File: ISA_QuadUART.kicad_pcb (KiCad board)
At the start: 2 copper layers, 104.1 x 102.9 mm, 41 parts, among them J1 ISA BUS, J11 Serial 4 IDC, J12 Serial 3 IDC, J13 UART4_SEL, J2 ADDR_IRQ, J3 UART1_SEL, J4 UART2_SEL, J5 ADDR, J7 Serial 1 DB9, J8 UART3_SEL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

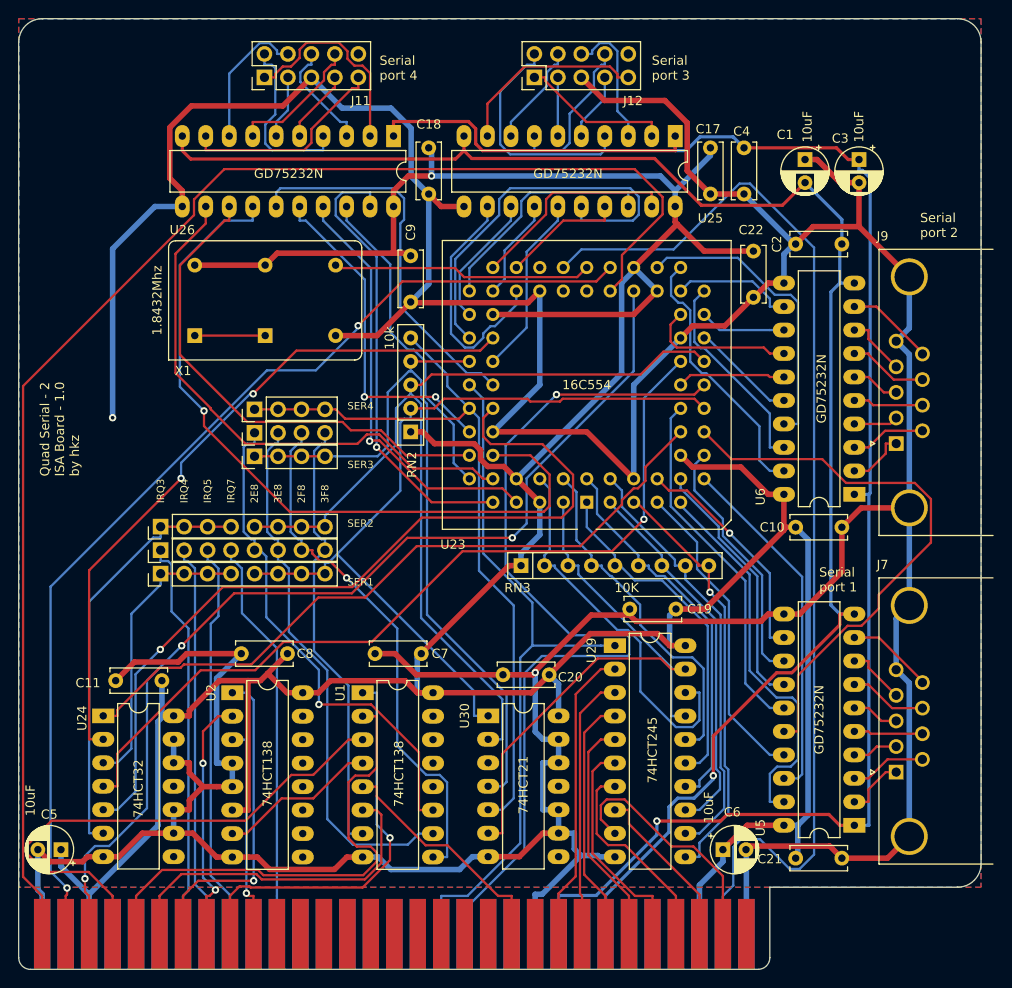
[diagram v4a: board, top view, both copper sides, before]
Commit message: Change ground plane on board
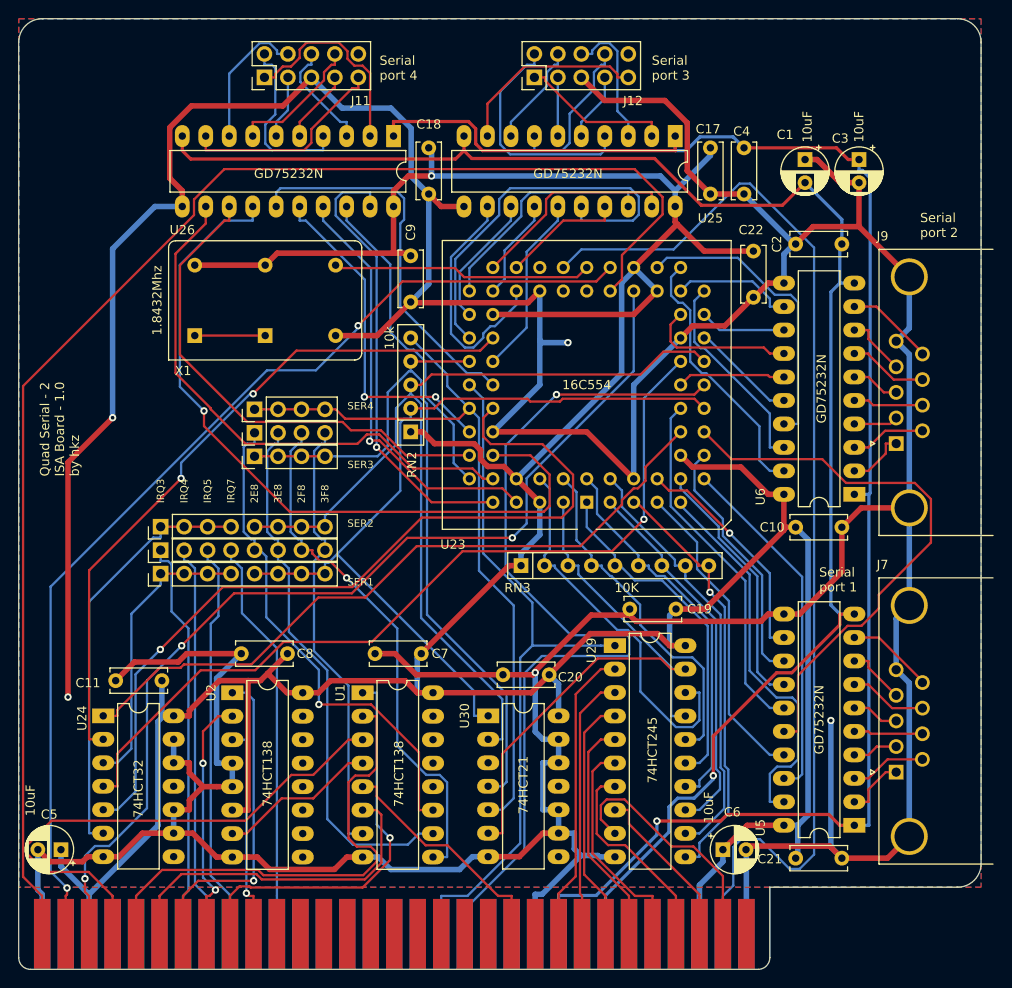
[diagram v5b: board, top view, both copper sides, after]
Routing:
- net GND: track 573.0 -> 623.8 mm, vias 2 -> 5

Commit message: Slight fixes to silkscreen
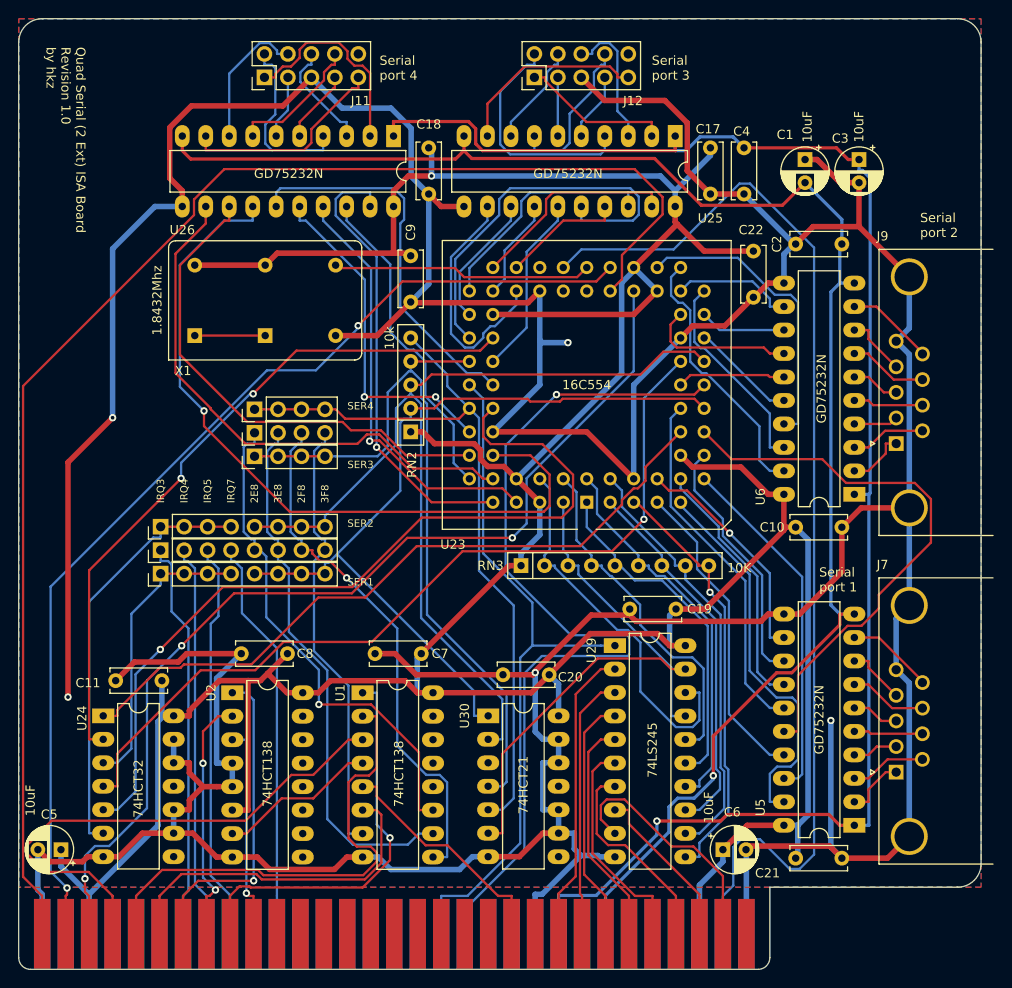
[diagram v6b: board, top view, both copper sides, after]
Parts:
- U29: value 74HCT245 -> 74LS245
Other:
- board text added: "Quad Serial (2 Ext) ISA Board Revision 1.0 by hkz"
- board text removed: "Quad Serial - 2 ISA Board - 1.0 by hkz"

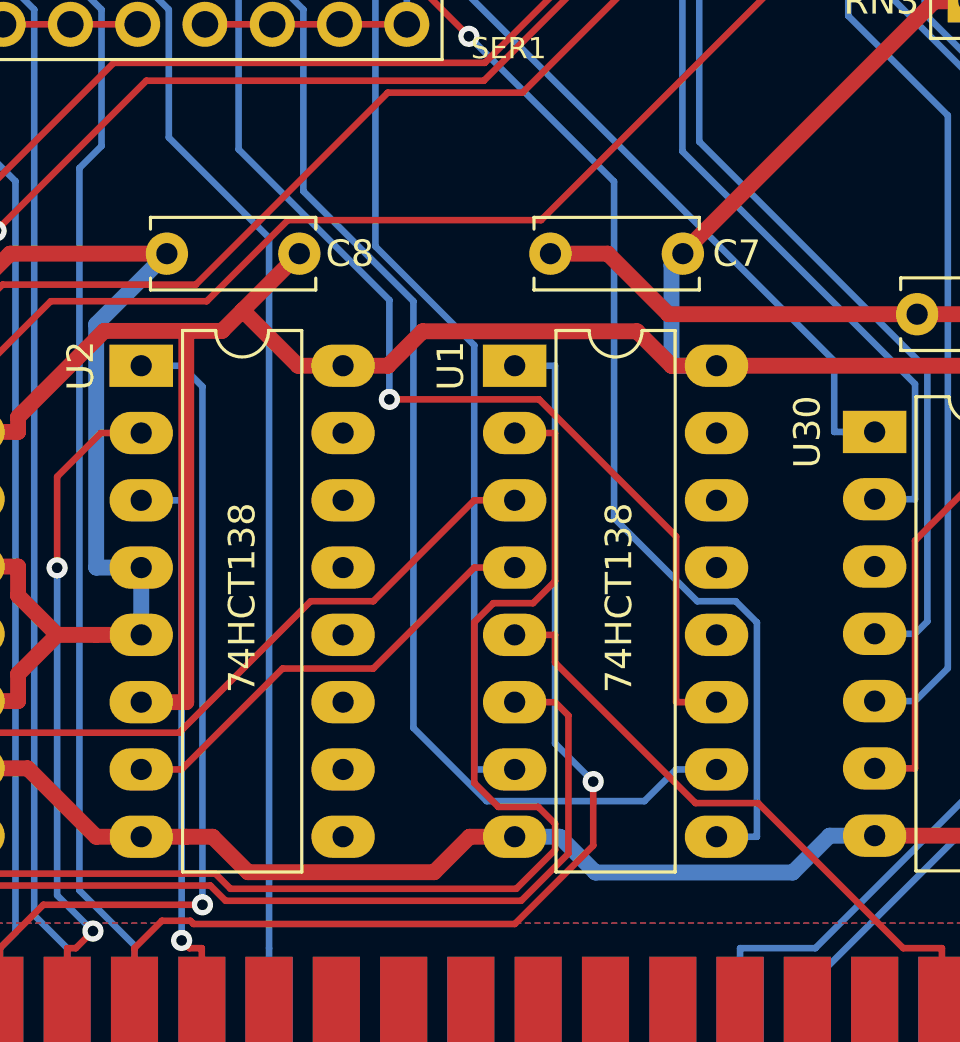
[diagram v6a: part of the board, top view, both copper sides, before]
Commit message: Slightly better filling for ground plane
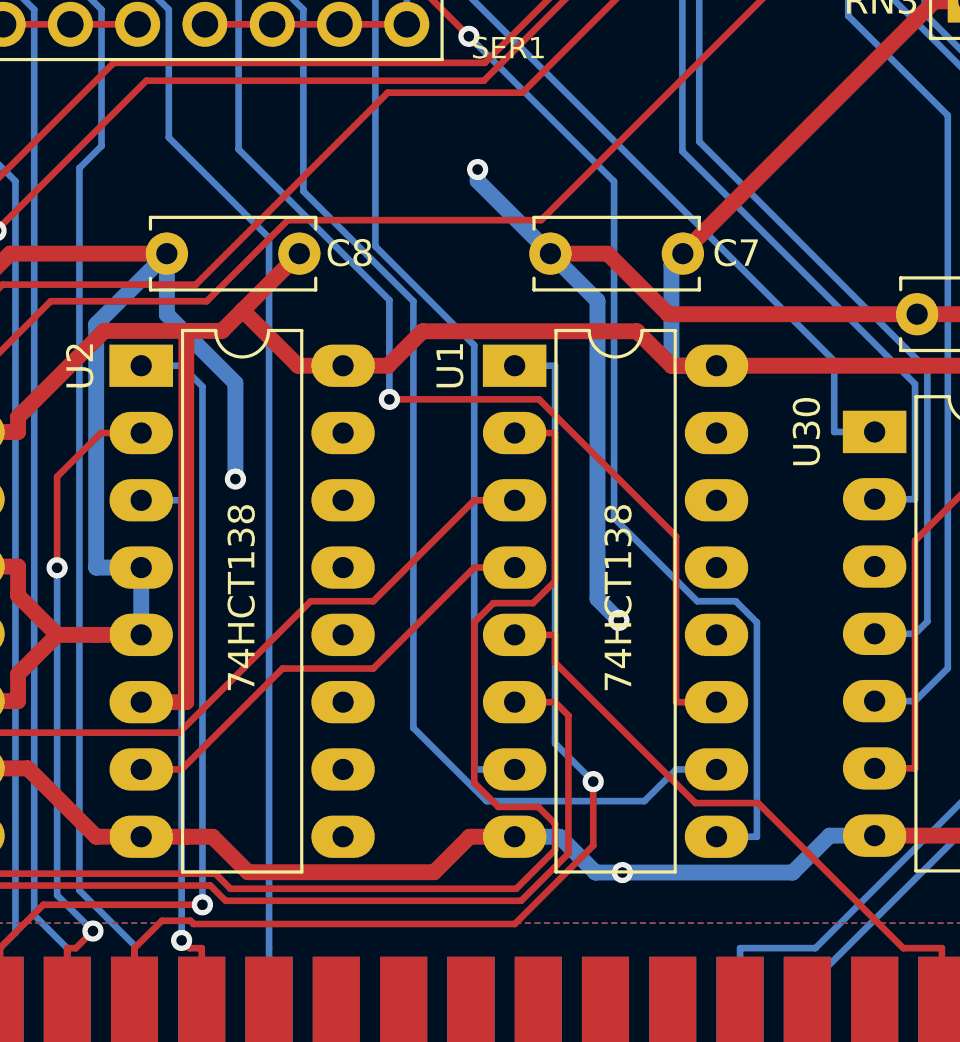
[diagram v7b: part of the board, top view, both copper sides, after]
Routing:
- net GND: track 623.8 -> 652.6 mm, vias 5 -> 9
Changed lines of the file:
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@@
     (thickness 1.6)
     (drawings 30)
-    (tracks 1300)
+    (tracks 1313)
     (zones 0)
     (modules 41)
@@
   (page A3)
   (layers
-    (0 F.Cu signal hide)
-    (31 B.Cu signal hide)
+    (0 F.Cu signal)
+    (31 B.Cu signal)
     (32 B.Adhes user)
     (33 F.Adhes user)
@@
   (segment (start 261.62 191.008) (end 259.9197 191.008) (width 0.6) (layer B.Cu) (net 2))
   (segment (start 259.9197 191.008) (end 258.5285 192.3992) (width 0.6) (layer B.Cu) (net 2))
-  (segment (start 258.5285 192.3992) (end 251.0825 192.3992) (width 0.6) (layer B.Cu) (net 2))
+  (segment (start 258.5285 192.3992) (end 252.1008 192.3992) (width 0.6) (layer B.Cu) (net 2))
   (segment (start 251.0825 192.3992) (end 249.7313 191.048) (width 0.6) (layer B.Cu) (net 2))
   (segment (start 246.3307 191.048) (end 244.9913 192.3874) (width 0.6) (layer F.Cu) (net 2))
@@
   (segment (start 216.154 148.336) (end 220.98 143.51) (width 0.6) (layer F.Cu) (net 2))
   (segment (start 216.154 173.736) (end 216.154 148.336) (width 0.6) (layer F.Cu) (net 2))
+  (via (at 246.634 165.862) (size 0.8) (drill 0.4) (layers F.Cu B.Cu) (net 2))
+  (segment (start 246.634 166.29) (end 249.381 169.037) (width 0.6) (layer B.Cu) (net 2))
+  (segment (start 246.634 165.862) (end 246.634 166.29) (width 0.6) (layer B.Cu) (net 2))
+  (via (at 251.968 182.88) (size 0.8) (drill 0.4) (layers F.Cu B.Cu) (net 2))
+  (segment (start 251.15819 170.81419) (end 249.381 169.037) (width 0.6) (layer B.Cu) (net 2))
+  (segment (start 251.15819 182.07019) (end 251.15819 170.81419) (width 0.6) (layer B.Cu) (net 2))
+  (segment (start 251.968 182.88) (end 251.15819 182.07019) (width 0.6) (layer B.Cu) (net 2))
+  (via (at 237.49 177.546) (size 0.8) (drill 0.4) (layers F.Cu B.Cu) (net 2))
+  (segment (start 234.903 171.336998) (end 234.903 169.037) (width 0.6) (layer B.Cu) (net 2))
+  (segment (start 237.49 173.923998) (end 234.903 171.336998) (width 0.6) (layer B.Cu) (net 2))
+  (segment (start 237.49 177.546) (end 237.49 173.923998) (width 0.6) (layer B.Cu) (net 2))
+  (segment (start 252.1008 192.3992) (end 251.0825 192.3992) (width 0.6) (layer B.Cu) (net 2))
+  (via (at 252.1008 192.3992) (size 0.8) (drill 0.4) (layers F.Cu B.Cu) (net 2))
   (segment (start 279.8802 187.1501) (end 279.8802 188.6329) (width 0.35) (layer B.Cu) (net 3))
   (segment (start 279.8802 188.6329) (end 273.3084 195.2047) (width 0.35) (layer B.Cu) (net 3))

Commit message: Add footprint for keystone 9200-15
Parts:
- added REF**: MNT_KEYSTONE_9200-15, Custom_Connectors:MNT_KEYSTONE_9200-15, F.Cu at (292.1, 195.6)
